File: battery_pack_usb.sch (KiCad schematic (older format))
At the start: 26 parts

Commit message: Annotate and assign
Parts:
- BT1, BT2: renamed from BT?; footprint (none) -> Connector_PinHeader_2.54mm:PinHeader_1x02_P2.54mm_Vertical
- C1, C4, C5: renamed from C?; footprint (none) -> Capacitor_SMD:C_0603_1608Metric_Pad1.05x0.95mm_HandSolder
- C2, C3, C6, C7, C8: renamed from C?; footprint (none) -> Capacitor_SMD:C_0805_2012Metric
- D1, D2: renamed from D?; footprint (none) -> LED_SMD:LED_0603_1608Metric_Pad1.05x0.95mm_HandSolder
- J1: renamed from J?; footprint (none) -> Connector_PinHeader_2.54mm:PinHeader_1x02_P2.54mm_Vertical
- J2: renamed from J?; footprint (none) -> Connector_USB:USB_C_Receptacle_Palconn_UTC16-G
- L1: renamed from L?; value L -> 1u; footprint (none) -> Inductor_SMD:L_1008_2520Metric; Name (none) -> DFE252012F-1R0M=P2
- R1, R2, R3, R4, R5, R6, R7, R8: renamed from R?; footprint (none) -> Resistor_SMD:R_0603_1608Metric_Pad1.05x0.95mm_HandSolder
- SW1: renamed from SW?; footprint (none) -> Connector_PinHeader_2.54mm:PinHeader_1x02_P2.54mm_Vertical
- TH1: renamed from TH?; footprint (none) -> Connector_PinHeader_2.54mm:PinHeader_1x02_P2.54mm_Vertical
- gave numbers to parts that had none: 1

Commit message: Finish PCB
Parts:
- removed BT1, BT2: Battery_Cell, Connector_PinHeader_2.54mm:PinHeader_1x02_P2.54mm_Vertical, symbol Device:Battery_Cell
- added BT1: Battery, Connector_PinHeader_2.54mm:PinHeader_1x02_P2.54mm_Vertical, symbol Device:Battery
- SW1, TH1: footprint Connector_PinHeader_2.54mm:PinHeader_1x02_P2.54mm_Vertical -> Connector_PinHeader_2.00mm:PinHeader_1x02_P2.00mm_Vertical
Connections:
- net BAT: now also BT1.1 (+)
- net GND: now also BT1.2 (-)
- net REGN: now also D1.2 (A), D2.2 (A); no longer R1.1, R2.1
- net D-: now reaches J2.A7 (D-), J2.B7 (D-), U1.1 (D-)
- net at U1.2 (STAT): now also R1.2; no longer D1.1 (K)
- net D+: now reaches J2.A6 (D+), J2.B6 (D+), U1.24 (D+)
- net at U1.9 (~PG): now also R2.2; no longer D2.1 (K)
- new net: D2.1 (K), R2.1
- new net: D1.1 (K), R1.1
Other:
- moved on the sheet: D1, D2, R1, R2
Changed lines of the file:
@@
 F 0 "SW1" H 4350 3550 50  0000 C CNN
 F 1 "SW_SPST" H 4350 3450 50  0000 C CNN
-F 2 "Connector_PinHeader_2.54mm:PinHeader_1x02_P2.54mm_Vertical" H 4350 3600 50  0001 C CNN
+F 2 "Connector_PinHeader_2.00mm:PinHeader_1x02_P2.00mm_Vertical" H 4350 3600 50  0001 C CNN
 F 3 "~" H 4350 3600 50  0001 C CNN
 	1    4350 3600
@@
 F 0 "TH1" H 7100 4050 50  0000 L CNN
 F 1 "103AT" V 7200 3750 50  0000 L CNN
-F 2 "Connector_PinHeader_2.54mm:PinHeader_1x02_P2.54mm_Vertical" H 7050 3950 50  0001 C CNN
+F 2 "Connector_PinHeader_2.00mm:PinHeader_1x02_P2.00mm_Vertical" H 7050 3950 50  0001 C CNN
 F 3 "~" H 7050 3950 50  0001 C CNN
 	1    7050 3900
@@
 $EndComp
 $Comp
-L Device:Battery_Cell BT1
-U 1 1 5F329931
-P 7350 3600
-F 0 "BT1" H 7468 3696 50  0000 L CNN
-F 1 "Battery_Cell" H 7468 3605 50  0000 L CNN
-F 2 "Connector_PinHeader_2.54mm:PinHeader_1x02_P2.54mm_Vertical" V 7350 3660 50  0001 C CNN
-F 3 "~" V 7350 3660 50  0001 C CNN
-	1    7350 3600
-	1    0    0    -1
-$EndComp
-$Comp
-L Device:Battery_Cell BT2
-U 1 1 5F329C9A
-P 7350 4000
-F 0 "BT2" H 7468 4096 50  0000 L CNN
-F 1 "Battery_Cell" H 7468 4005 50  0000 L CNN
-F 2 "Connector_PinHeader_2.54mm:PinHeader_1x02_P2.54mm_Vertical" V 7350 4060 50  0001 C CNN
-F 3 "~" V 7350 4060 50  0001 C CNN
-	1    7350 4000
-	1    0    0    -1
-$EndComp
-$Comp
 L power:GND #PWR010
 U 1 1 5F32A858
@@
 $EndComp
 Wire Wire Line
-	7350 4150 7350 4100
-Wire Wire Line
-	7350 3800 7350 3700
-Wire Wire Line
 	6350 3700 6350 3600
 Wire Wire Line
@@
 Wire Wire Line
 	6450 3300 7100 3300
-Wire Wire Line
-	7350 3300 7350 3400
 $Comp
 L Device:C C6
@@
 L Device:LED D2
 U 1 1 5F35D60D
+P 6350 2100
+F 0 "D2" H 6250 2100 50  0000 C CNN
+F 1 "LED" H 6500 2050 50  0000 C CNN
+F 2 "LED_SMD:LED_0603_1608Metric_Pad1.05x0.95mm_HandSolder" H 6350 2100 50  0001 C CNN
+F 3 "~" H 6350 2100 50  0001 C CNN
+	1    6350 2100
+	0    -1   -1   0
+$EndComp
+$Comp
+L Device:LED D1
+U 1 1 5F35E5EE
+P 6150 2100
+F 0 "D1" H 6050 2100 50  0000 C CNN
+F 1 "LED" H 6300 2050 50  0000 C CNN
+F 2 "LED_SMD:LED_0603_1608Metric_Pad1.05x0.95mm_HandSolder" H 6150 2100 50  0001 C CNN
+F 3 "~" H 6150 2100 50  0001 C CNN
+	1    6150 2100
+	0    -1   -1   0
+$EndComp
+Wire Wire Line
+	6100 2650 6150 2650
+Wire Wire Line
+	6150 2650 6150 2600
+Wire Wire Line
+	6100 2750 6350 2750
+Wire Wire Line
+	6350 2750 6350 2600
+$Comp
+L Device:R R1
+U 1 1 5F368F5A
+P 6150 2450
+F 0 "R1" H 6220 2496 50  0000 L CNN
+F 1 "R" H 6220 2405 50  0000 L CNN
+F 2 "Resistor_SMD:R_0603_1608Metric_Pad1.05x0.95mm_HandSolder" V 6080 2450 50  0001 C CNN
+F 3 "~" H 6150 2450 50  0001 C CNN
+	1    6150 2450
+	1    0    0    -1
+$EndComp
+$Comp
+L Device:R R2
+U 1 1 5F36928A
 P 6350 2450
-F 0 "D2" H 6250 2450 50  0000 C CNN
-F 1 "LED" H 6500 2400 50  0000 C CNN
-F 2 "LED_SMD:LED_0603_1608Metric_Pad1.05x0.95mm_HandSolder" H 6350 2450 50  0001 C CNN
+F 0 "R2" H 6420 2496 50  0000 L CNN
+F 1 "R" H 6420 2405 50  0000 L CNN
+F 2 "Resistor_SMD:R_0603_1608Metric_Pad1.05x0.95mm_HandSolder" V 6280 2450 50  0001 C CNN
 F 3 "~" H 6350 2450 50  0001 C CNN
 	1    6350 2450
-	0    -1   -1   0
-$EndComp
-$Comp
-L Device:LED D1
-U 1 1 5F35E5EE
-P 6150 2450
-F 0 "D1" H 6050 2450 50  0000 C CNN
-F 1 "LED" H 6300 2400 50  0000 C CNN
-F 2 "LED_SMD:LED_0603_1608Metric_Pad1.05x0.95mm_HandSolder" H 6150 2450 50  0001 C CNN
-F 3 "~" H 6150 2450 50  0001 C CNN
-	1    6150 2450
-	0    -1   -1   0
-$EndComp
-Wire Wire Line
-	6100 2650 6150 2650
-Wire Wire Line
-	6150 2650 6150 2600
-Wire Wire Line
-	6100 2750 6350 2750
-Wire Wire Line
-	6350 2750 6350 2600
-$Comp
-L Device:R R1
-U 1 1 5F368F5A
-P 6150 2100
-F 0 "R1" H 6220 2146 50  0000 L CNN
-F 1 "R" H 6220 2055 50  0000 L CNN
-F 2 "Resistor_SMD:R_0603_1608Metric_Pad1.05x0.95mm_HandSolder" V 6080 2100 50  0001 C CNN
-F 3 "~" H 6150 2100 50  0001 C CNN
-	1    6150 2100
-	1    0    0    -1
-$EndComp
-$Comp
-L Device:R R2
-U 1 1 5F36928A
-P 6350 2100
-F 0 "R2" H 6420 2146 50  0000 L CNN
-F 1 "R" H 6420 2055 50  0000 L CNN
-F 2 "Resistor_SMD:R_0603_1608Metric_Pad1.05x0.95mm_HandSolder" V 6280 2100 50  0001 C CNN
-F 3 "~" H 6350 2100 50  0001 C CNN
-	1    6350 2100
 	1    0    0    -1
 $EndComp
@@
 	3850 2200 3850 2250
 Connection ~ 3850 2250
+$Comp
+L Device:Battery BT1
+U 1 1 5F3AAE8C
+P 7350 3750
+F 0 "BT1" H 7458 3796 50  0000 L CNN
+F 1 "Battery" H 7458 3705 50  0000 L CNN
+F 2 "Connector_PinHeader_2.54mm:PinHeader_1x02_P2.54mm_Vertical" V 7350 3810 50  0001 C CNN
+F 3 "~" V 7350 3810 50  0001 C CNN
+	1    7350 3750
+	1    0    0    -1
+$EndComp
+Wire Wire Line
+	7350 3950 7350 4150
+Wire Wire Line
+	7350 3300 7350 3550
+Text Label 3750 3400 0    50   ~ 0
+D+
+Text Label 3750 3200 0    50   ~ 0
+D-
 $EndSCHEMATC

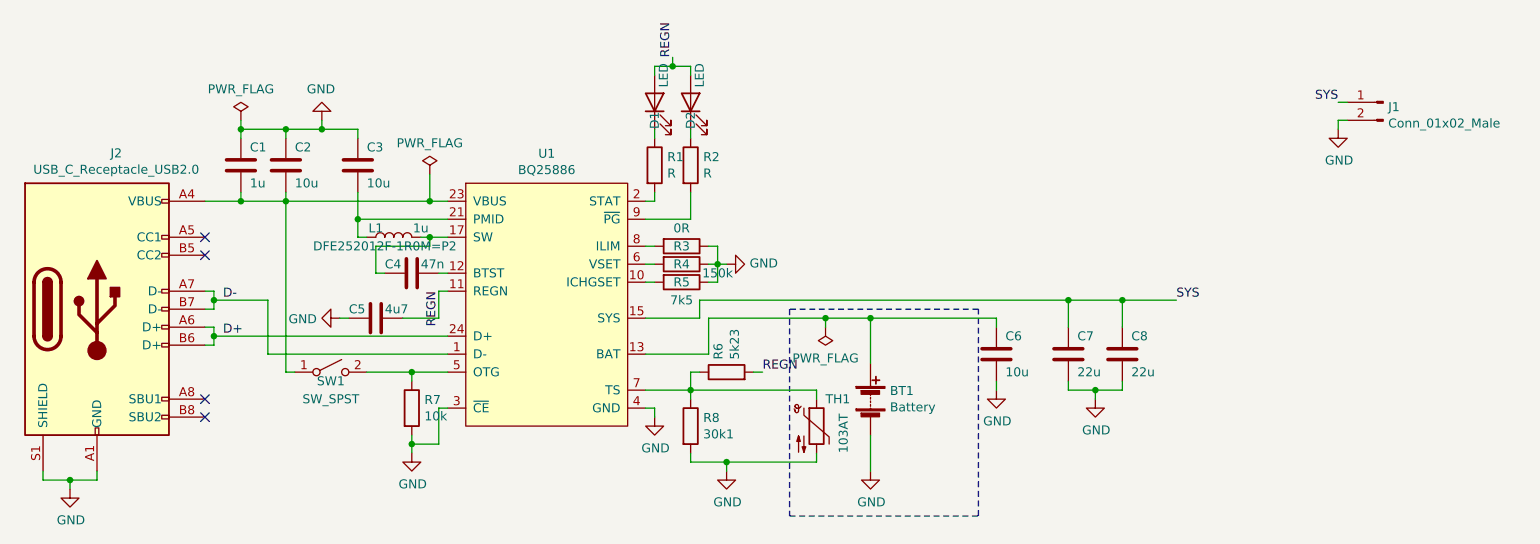
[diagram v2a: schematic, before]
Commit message: Add voltages to capacitances
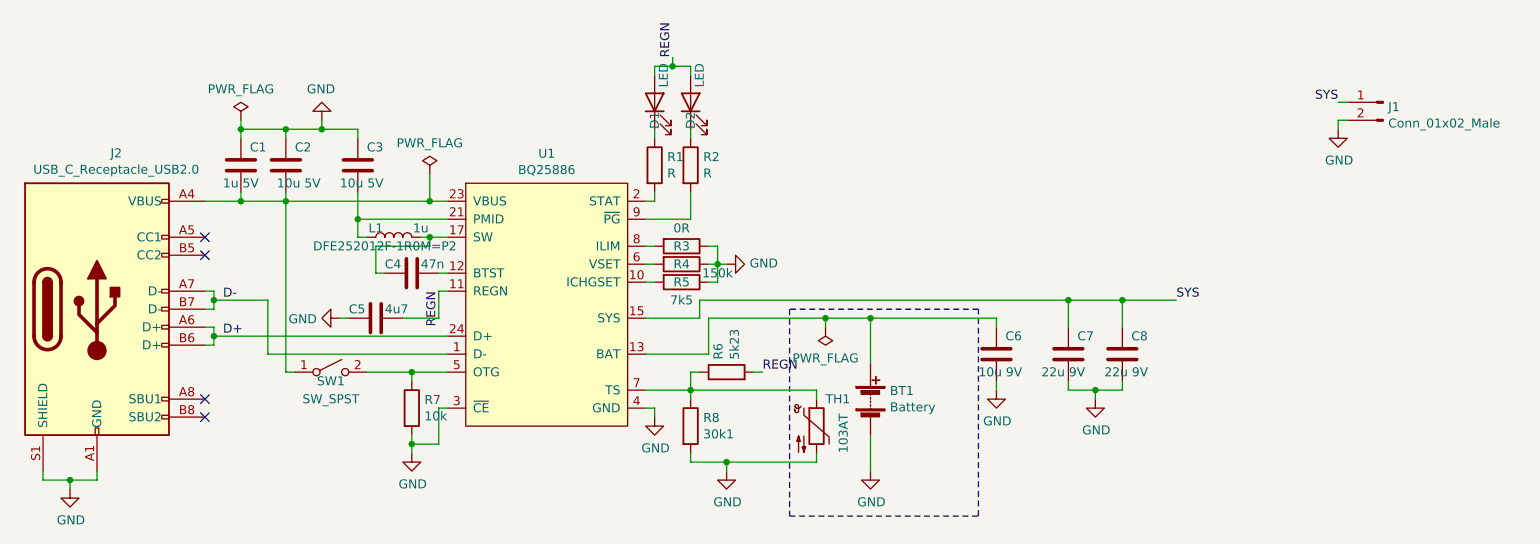
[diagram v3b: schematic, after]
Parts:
- C1: value 1u -> 1u 5V
- C2, C3: value 10u -> 10u 5V
- C6: value 10u -> 10u 9V
- C7, C8: value 22u -> 22u 9V
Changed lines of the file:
@@
 P 4100 2450
 F 0 "C2" H 4150 2550 50  0000 L CNN
-F 1 "10u" H 4150 2350 50  0000 L CNN
+F 1 "10u 5V" H 4050 2350 50  0000 L CNN
 F 2 "Capacitor_SMD:C_0805_2012Metric" H 4138 2300 50  0001 C CNN
 F 3 "~" H 4100 2450 50  0001 C CNN
@@
 P 4500 2450
 F 0 "C3" H 4550 2550 50  0000 L CNN
-F 1 "10u" H 4550 2350 50  0000 L CNN
+F 1 "10u 5V" H 4400 2350 50  0000 L CNN
 F 2 "Capacitor_SMD:C_0805_2012Metric" H 4538 2300 50  0001 C CNN
 F 3 "~" H 4500 2450 50  0001 C CNN
@@
 P 8050 3500
 F 0 "C6" H 8100 3600 50  0000 L CNN
-F 1 "10u" H 8100 3400 50  0000 L CNN
+F 1 "10u 9V" H 7950 3400 50  0000 L CNN
 F 2 "Capacitor_SMD:C_0805_2012Metric" H 8088 3350 50  0001 C CNN
 F 3 "~" H 8050 3500 50  0001 C CNN
@@
 P 3850 2450
 F 0 "C1" H 3900 2550 50  0000 L CNN
-F 1 "1u" H 3900 2350 50  0000 L CNN
+F 1 "1u 5V" H 3750 2350 50  0000 L CNN
 F 2 "Capacitor_SMD:C_0603_1608Metric_Pad1.05x0.95mm_HandSolder" H 3888 2300 50  0001 C CNN
 F 3 "~" H 3850 2450 50  0001 C CNN
@@
 P 8450 3500
 F 0 "C7" H 8500 3600 50  0000 L CNN
-F 1 "22u" H 8500 3400 50  0000 L CNN
+F 1 "22u 9V" H 8300 3400 50  0000 L CNN
 F 2 "Capacitor_SMD:C_0805_2012Metric" H 8488 3350 50  0001 C CNN
 F 3 "~" H 8450 3500 50  0001 C CNN
@@
 P 8750 3500
 F 0 "C8" H 8800 3600 50  0000 L CNN
-F 1 "22u" H 8800 3400 50  0000 L CNN
+F 1 "22u 9V" H 8650 3400 50  0000 L CNN
 F 2 "Capacitor_SMD:C_0805_2012Metric" H 8788 3350 50  0001 C CNN
 F 3 "~" H 8750 3500 50  0001 C CNN
